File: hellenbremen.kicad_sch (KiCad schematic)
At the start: 11 parts, among them M2 Module-power_12and5V-0.2

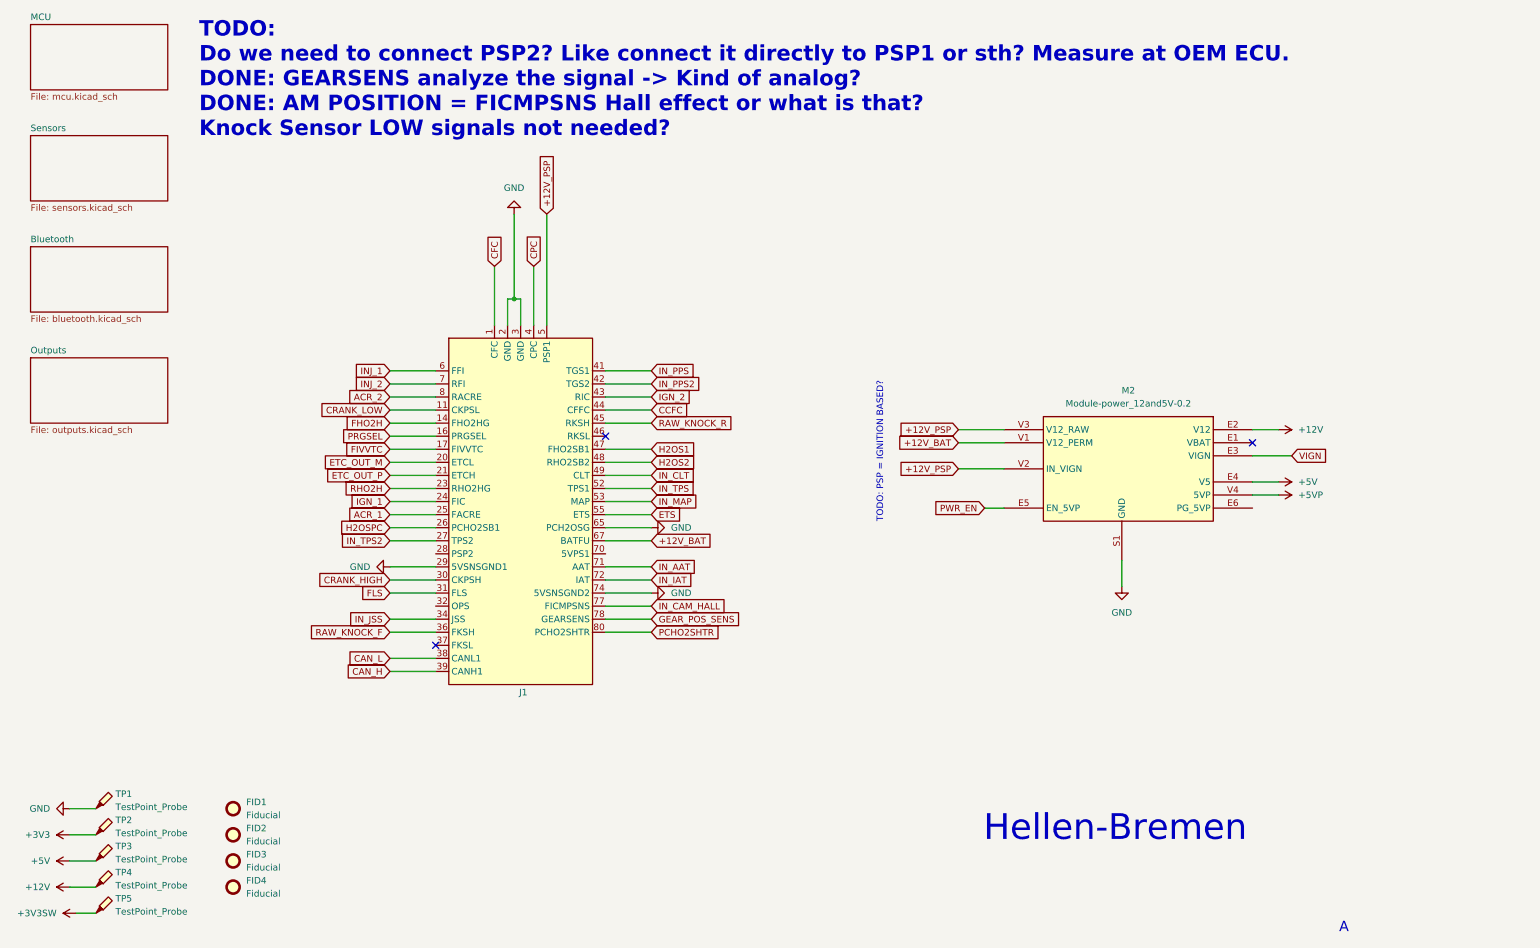
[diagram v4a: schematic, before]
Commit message: ccfc mosfet and power changes
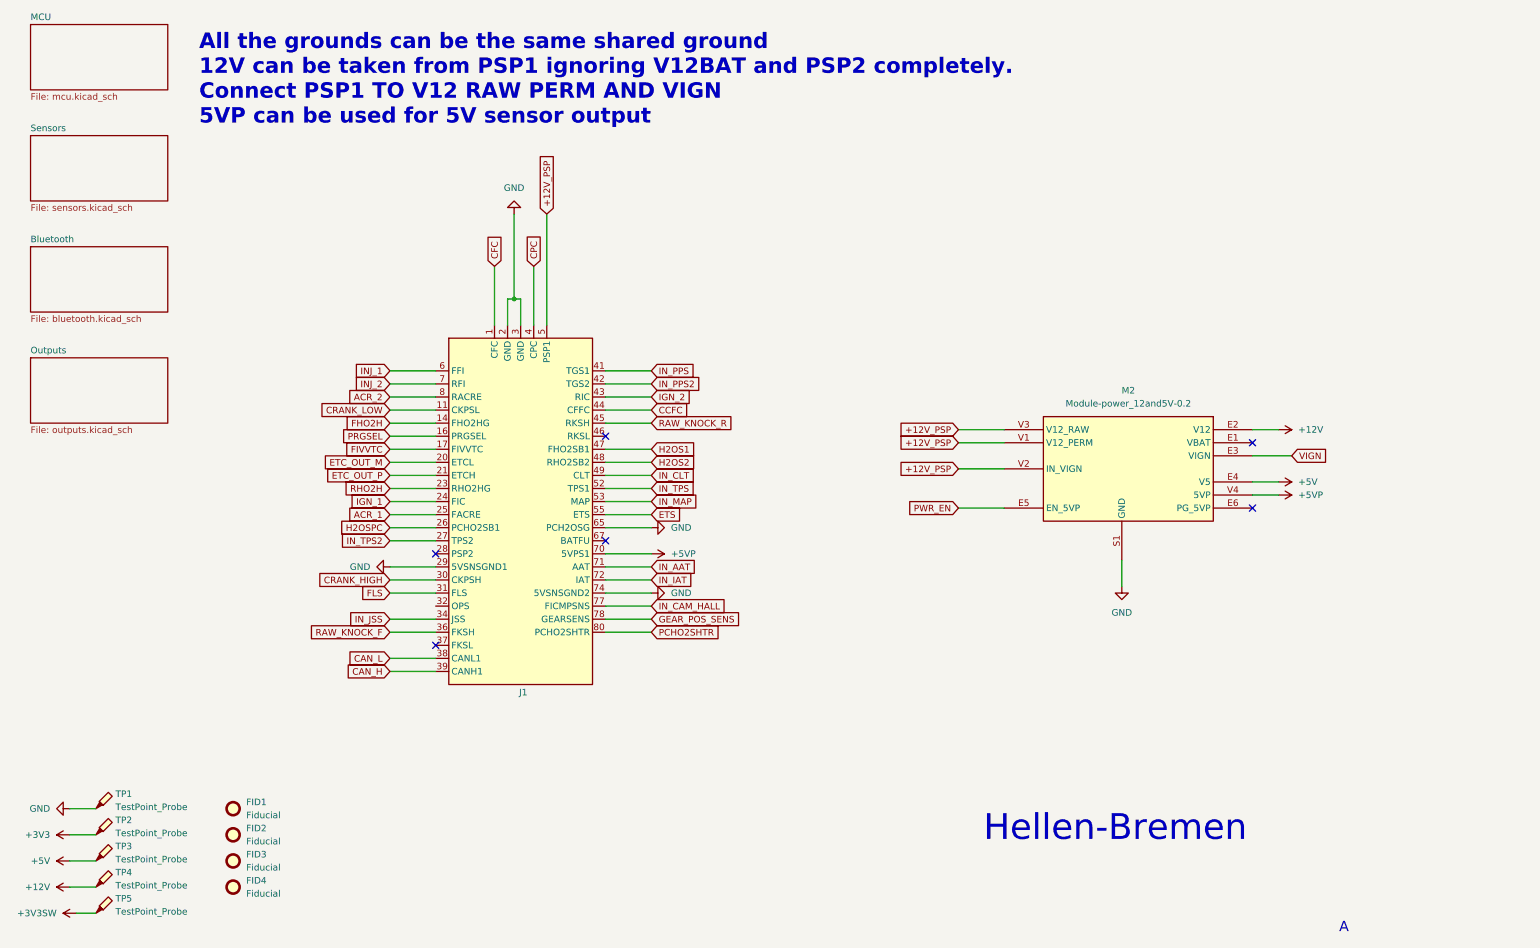
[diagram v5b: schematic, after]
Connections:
- net +12V_PSP: now also M2.V1 (V12_PERM)
- net +5VP: now also J1.70 (5VPS1)
- net +12V_BAT: no longer names the net of J1.67 (BATFU)
- net +12V_BAT: no longer M2.V1 (V12_PERM)
- no-connect marks 3 -> 6
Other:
- note added: "All the grounds can be the same shared ground 12V can be taken from PSP1 ignoring V12BAT and PSP2 completely. Connect PSP1 TO V12 RAW PERM AND VIGN 5VP can be used for 5V sensor output"
- note removed: "TODO: Do we need to connect PSP2? Like connect it directly to PSP1 or sth? Measure at OEM ECU. DONE: GEARSENS analyze the signal -> Kind of analog? DONE: AM POSITION = FICMPSNS Hall effect or what is that? Knock Sensor LOW signals not needed?"
- note removed: "TODO: PSP = IGNITION BASED?"
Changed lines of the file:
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@@
+	)
+	(no_connect
+		(at 93.98 120.65)
+	)
+	(no_connect
+		(at 127 118.11)
+	)
+	(no_connect
+		(at 252.73 111.76)
 	)
 	(no_connect
@@
 	(wire
 		(pts
+			(xy 127 120.65) (xy 135.89 120.65)
+		)
+		(stroke
+			(width 0)
+			(type default)
+		)
+	)
+	(wire
+		(pts
 			(xy 22.86 185.42) (xy 27.94 185.42)
 		)
@@
 	(wire
 		(pts
-			(xy 200.66 111.76) (xy 204.47 111.76)
+			(xy 195.58 111.76) (xy 204.47 111.76)
 		)
 		(stroke
@@
 	(wire
 		(pts
-			(xy 127 118.11) (xy 135.89 118.11)
-		)
-		(stroke
-			(width 0)
-			(type default)
-		)
-	)
-	(wire
-		(pts
 			(xy 93.98 135.89) (xy 85.09 135.89)
 		)
@@
 		)
 	)
-	(text "TODO: PSP = IGNITION BASED?"
-		(exclude_from_sim no)
-		(at 180.34 100.838 90)
-		(effects
-			(font
-				(size 1.27 1.27)
-			)
-		)
-	)
-	(text "TODO:\nDo we need to connect PSP2? Like connect it directly to PSP1 or sth? Measure at OEM ECU.\nDONE: GEARSENS analyze the signal -> Kind of analog?\nDONE: AM POSITION = FICMPSNS Hall effect or what is that?\nKnock Sensor LOW signals not needed?\n"
+	(text "All the grounds can be the same shared ground\n12V can be taken from PSP1 ignoring V12BAT and PSP2 completely.\nConnect PSP1 TO V12 RAW PERM AND VIGN\n5VP can be used for 5V sensor output"
 		(exclude_from_sim no)
 		(at 48.006 28.448 0)
@@
 	(global_label "PWR_EN"
 		(shape input)
-		(at 200.66 111.76 180)
-		(fields_autoplaced yes)
-		(effects
-			(font
-				(size 1.27 1.27)
-			)
-			(justify right)
-		)
-		(property "Intersheetrefs" "${INTERSHEET_REFS}"
-			(at 190.2363 111.76 0)
+		(at 195.58 111.76 180)
+		(fields_autoplaced yes)
+		(effects
+			(font
+				(size 1.27 1.27)
+			)
+			(justify right)
+		)
+		(property "Intersheetrefs" "${INTERSHEET_REFS}"
+			(at 185.1563 111.76 0)
 			(effects
 				(font
@@
 		)
 	)
+	(global_label "+12V_PSP"
+		(shape input)
+		(at 195.58 99.06 180)
+		(fields_autoplaced yes)
+		(effects
+			(font
+				(size 1.27 1.27)
+			)
+			(justify right)
+		)
+		(property "Intersheetrefs" "${INTERSHEET_REFS}"
+			(at 182.7977 99.06 0)
+			(effects
+				(font
+					(size 1.27 1.27)
+				)
+				(justify right)
+				(hide yes)
+			)
+		)
+	)
 	(global_label "IN_PPS2"
 		(shape input)
@@
 		)
 	)
-	(global_label "+12V_BAT"
-		(shape input)
-		(at 135.89 118.11 0)
-		(fields_autoplaced yes)
-		(effects
-			(font
-				(size 1.27 1.27)
-			)
-			(justify left)
-		)
-		(property "Intersheetrefs" "${INTERSHEET_REFS}"
-			(at 148.249 118.11 0)
-			(effects
-				(font
-					(size 1.27 1.27)
-				)
-				(justify left)
-				(hide yes)
-			)
-		)
-	)
 	(global_label "IN_IAT"
 		(shape input)
@@
 				)
 				(justify left)
-				(hide yes)
-			)
-		)
-	)
-	(global_label "+12V_BAT"
-		(shape input)
-		(at 195.58 99.06 180)
-		(fields_autoplaced yes)
-		(effects
-			(font
-				(size 1.27 1.27)
-			)
-			(justify right)
-		)
-		(property "Intersheetrefs" "${INTERSHEET_REFS}"
-			(at 183.221 99.06 0)
-			(effects
-				(font
-					(size 1.27 1.27)
-				)
-				(justify right)
 				(hide yes)
 			)
@@
 					(unit 1)
 				)
+			)
+		)
+	)
+	(symbol
+		(lib_id "power:+5VP")
+		(at 135.89 120.65 270)
+		(unit 1)
+		(exclude_from_sim no)
+		(in_bom yes)
+		(on_board yes)
+		(dnp no)
+		(fields_autoplaced yes)
+		(property "Reference" "#PWR084"
+			(at 132.08 120.65 0)
+			(effects
+				(font
+					(size 1.27 1.27)
+				)
+				(hide yes)
+			)
+		)
+		(property "Value" "+5VP"
+			(at 139.7 120.6499 90)
+			(effects
+				(font
+					(size 1.27 1.27)
+				)
+				(justify left)
+			)
+		)
+		(property "Footprint" ""
+			(at 135.89 120.65 0)
+			(effects
+				(font
+					(size 1.27 1.27)
+				)
+				(hide yes)
+			)
+		)
+		(property "Datasheet" ""
+			(at 135.89 120.65 0)
+			(effects
+				(font
+					(size 1.27 1.27)
+				)
+				(hide yes)
+			)
+		)
+		(property "Description" "Power symbol creates a global label with name \"+5VP\""
+			(at 135.89 120.65 0)
+			(effects
+				(font
+					(size 1.27 1.27)
+				)
+				(hide yes)
+			)
+		)
+		(pin "1"
+		)
+		(instances
+			(project "hellenbremen"
+				(path "/83409e39-90d0-4c85-be2e-bd292bea7c12"
+					(reference "#PWR084")
+					(unit 1)
+				)

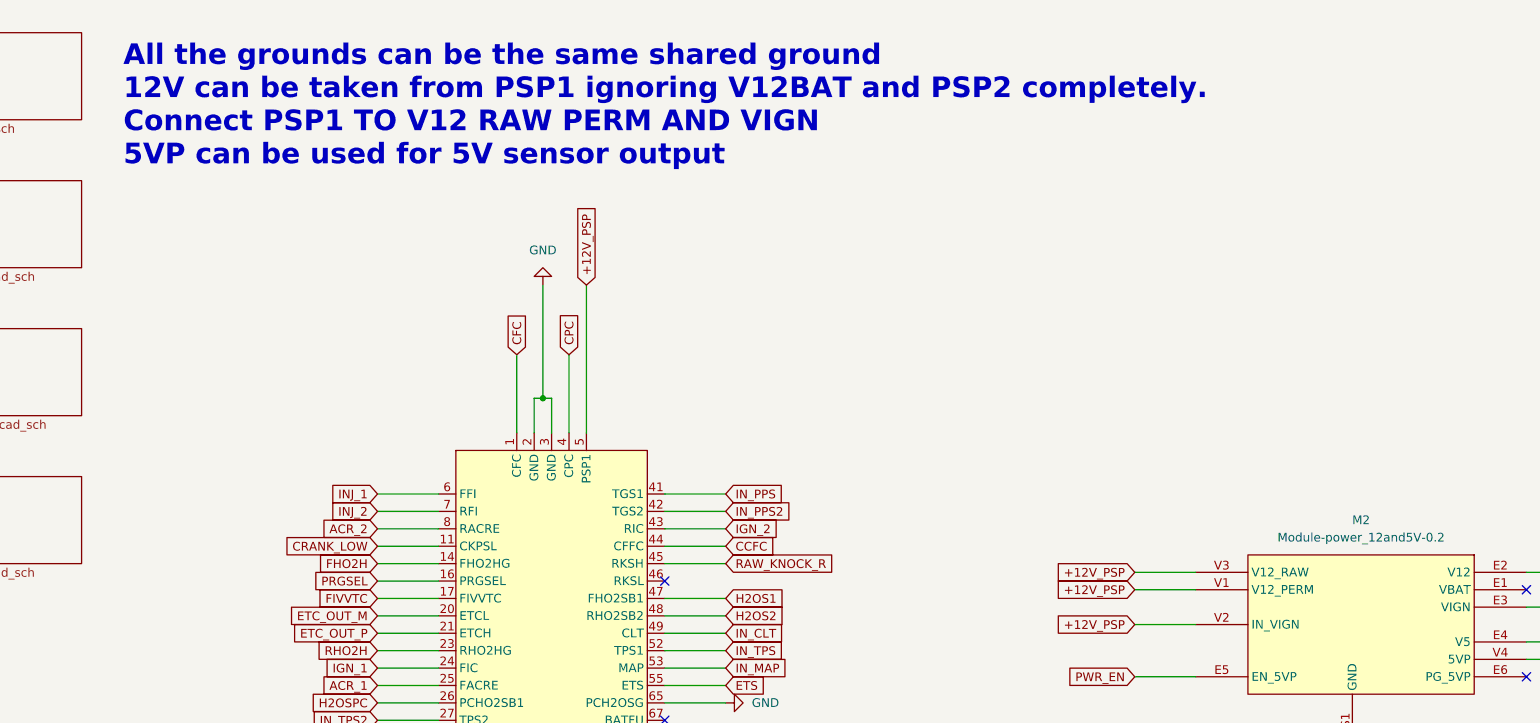
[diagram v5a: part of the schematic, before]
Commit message: no perm 12V and minor routing
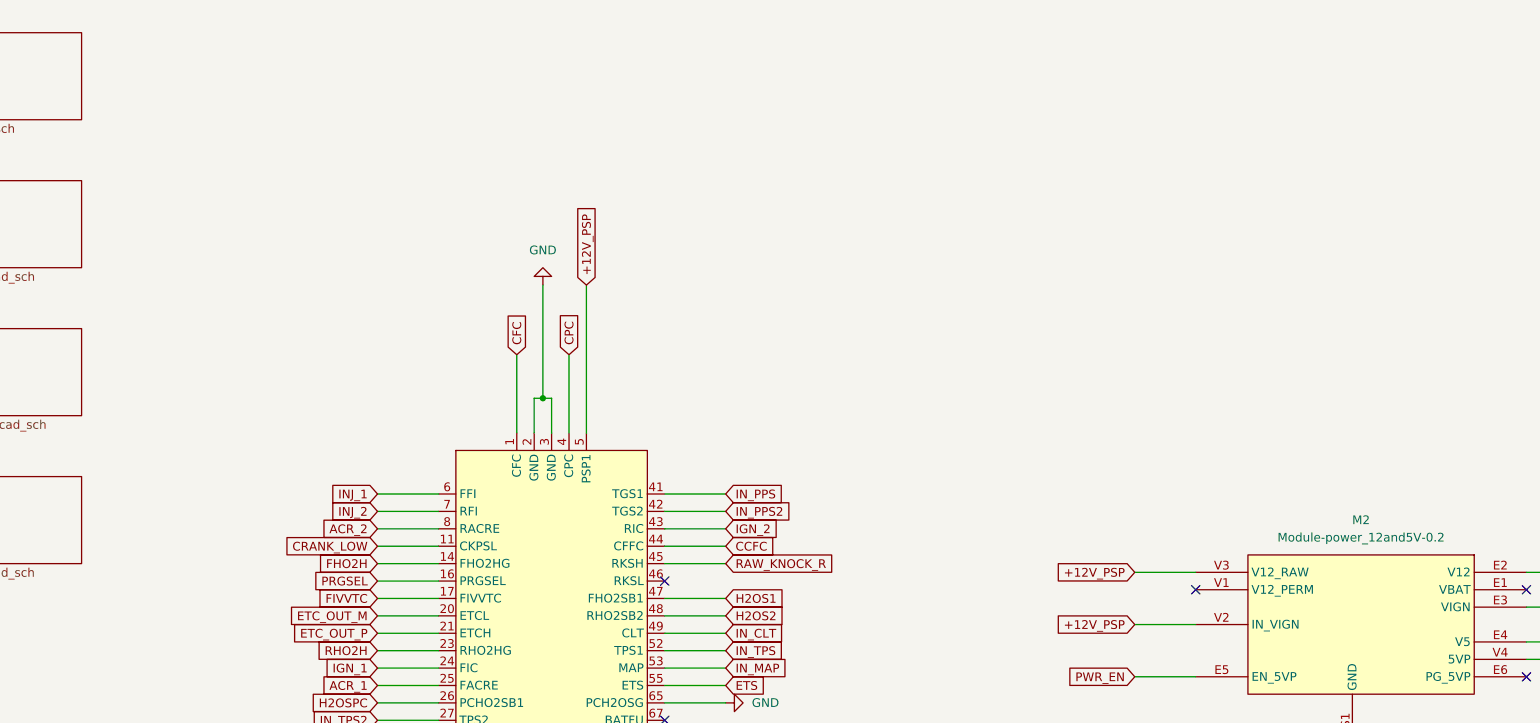
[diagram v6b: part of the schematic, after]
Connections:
- net +12V_PSP: no longer M2.V1 (V12_PERM)
- no-connect marks 6 -> 7
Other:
- note removed: "All the grounds can be the same shared ground 12V can be taken from PSP1 ignoring V12BAT and PSP2 completely. Connect PSP1 TO V12 RAW PERM AND VIGN 5VP can be used for 5V sensor output"
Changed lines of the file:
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@@
+	)
+	(no_connect
+		(at 204.47 99.06)
 	)
 	(no_connect
@@
 	(wire
 		(pts
-			(xy 195.58 99.06) (xy 204.47 99.06)
-		)
-		(stroke
-			(width 0)
-			(type default)
-		)
-	)
-	(wire
-		(pts
 			(xy 127 95.25) (xy 135.89 95.25)
 		)
@@
 			(width 0)
 			(type default)
-		)
-	)
-	(text "All the grounds can be the same shared ground\n12V can be taken from PSP1 ignoring V12BAT and PSP2 completely.\nConnect PSP1 TO V12 RAW PERM AND VIGN\n5VP can be used for 5V sensor output"
-		(exclude_from_sim no)
-		(at 48.006 28.448 0)
-		(effects
-			(font
-				(size 3 3)
-				(thickness 0.6)
-				(bold yes)
-			)
-			(justify left)
 		)
 	)
@@
 				(hide yes)
 			)
-		)
-	)
-	(global_label "+12V_PSP"
-		(shape input)
-		(at 195.58 99.06 180)
-		(fields_autoplaced yes)
-		(effects
-			(font
-				(size 1.27 1.27)
-			)
-			(justify right)
-		)
-		(property "Intersheetrefs" "${INTERSHEET_REFS}"
-			(at 182.7977 99.06 0)
-			(effects
-				(font
-					(size 1.27 1.27)
-				)
-				(justify right)
-				(hide yes)
-			)
